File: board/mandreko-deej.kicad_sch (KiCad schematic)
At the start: 22 parts, among them U1 ProMicroC

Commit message: Fixed footprints of sliders, after verifying original was incorrect. Routed wires. Generated fabrication outputs
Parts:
- R1, R2, R3, R4, R5: footprint POT_PTA6043 -> Bourns:PTA6043-2015DP-B103; symbol Bourns:PTA6043-2015DPB103 -> Bourns:PTA6043-2015DP-B103; Availability (none) -> In Stock; Check_prices (none) -> https://www.snapeda.com/parts/PTA6043-2015DPB103/Bourns/vie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; Description_1 (none) -> PTA Series, Linear Potentiometer, 10kOhms, +/-20%, 0.25W, T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; MF (none) -> Bourns; MP (none) -> PTA6043-2015DPB103; Package (none) -> None; Price (none) -> None; SnapEDA_Link (none) -> https://www.snapeda.com/parts/PTA6043-2015DPB103/Bourns/vie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
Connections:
- net GND: now also R1.3, R2.3, R3.3, R4.3, R5.3; no longer R1.1, R2.1, R3.1, R4.1, R5.1
- net at S4.1: now also R4.1; no longer R4.3
- net at S3.1: now also R3.1; no longer R3.3
- net at D2.2 (DOUT): now also D3.4 (DIN)
- net at S1.1: now also R1.1; no longer R1.3
- net at S2.1: now also R2.1; no longer R2.3
- net at S5.1: now also R5.1; no longer R5.3

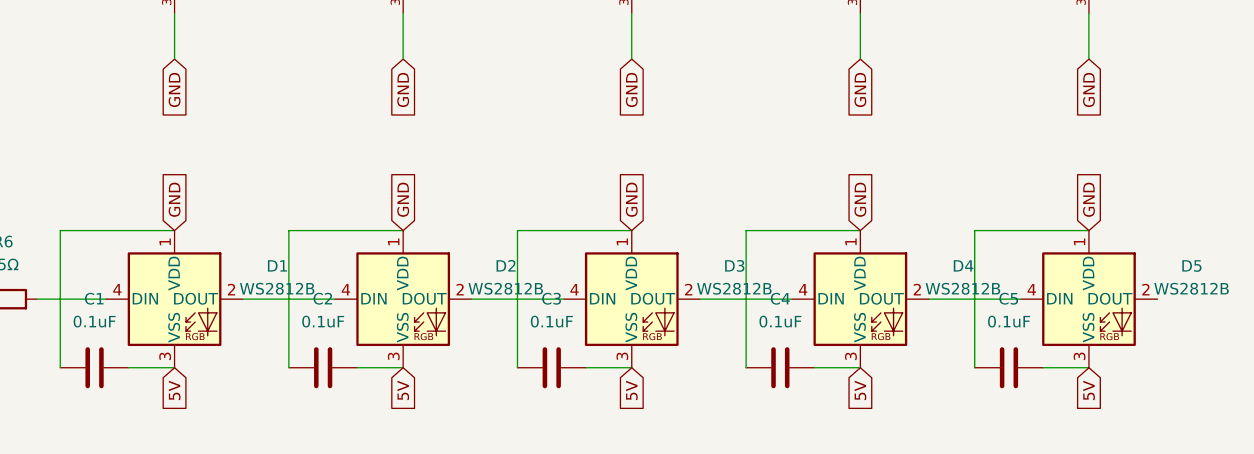
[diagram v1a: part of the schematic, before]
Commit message: Fixed board wiring error. Regenerated fabrication files. Added PlatformIO project with LED code. Added STEP of the board 3d model.
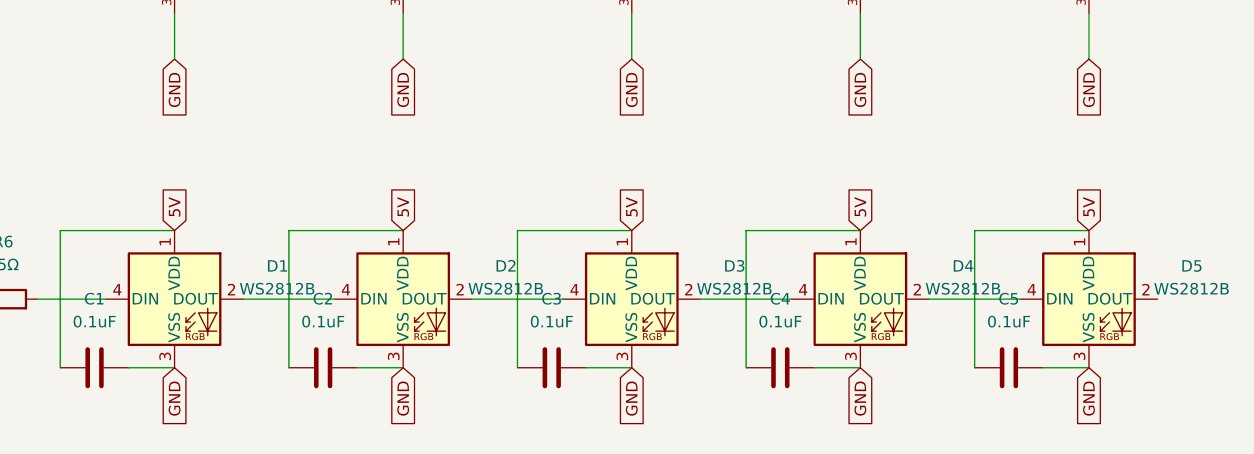
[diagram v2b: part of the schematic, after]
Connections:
- net 5V: now also C1.1, C2.1, C3.1, C4.1, C5.1, D1.1 (VDD), D2.1 (VDD), D3.1 (VDD), D4.1 (VDD), D5.1 (VDD); no longer C1.2, C2.2, C3.2, C4.2, C5.2, D1.3 (VSS), D2.3 (VSS), D3.3 (VSS), D4.3 (VSS), D5.3 (VSS)
- net GND: now also C1.2, C2.2, C3.2, C4.2, C5.2, D1.3 (VSS), D2.3 (VSS), D3.3 (VSS), D4.3 (VSS), D5.3 (VSS); no longer C1.1, C2.1, C3.1, C4.1, C5.1, D1.1 (VDD), D2.1 (VDD), D3.1 (VDD), D4.1 (VDD), D5.1 (VDD)
